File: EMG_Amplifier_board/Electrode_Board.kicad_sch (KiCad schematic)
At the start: 0 parts

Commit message: pcb design v1
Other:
- sheet input_protection_and_decoupling ports: added none; removed GND
- sheet output_protection ports: added none; removed GND

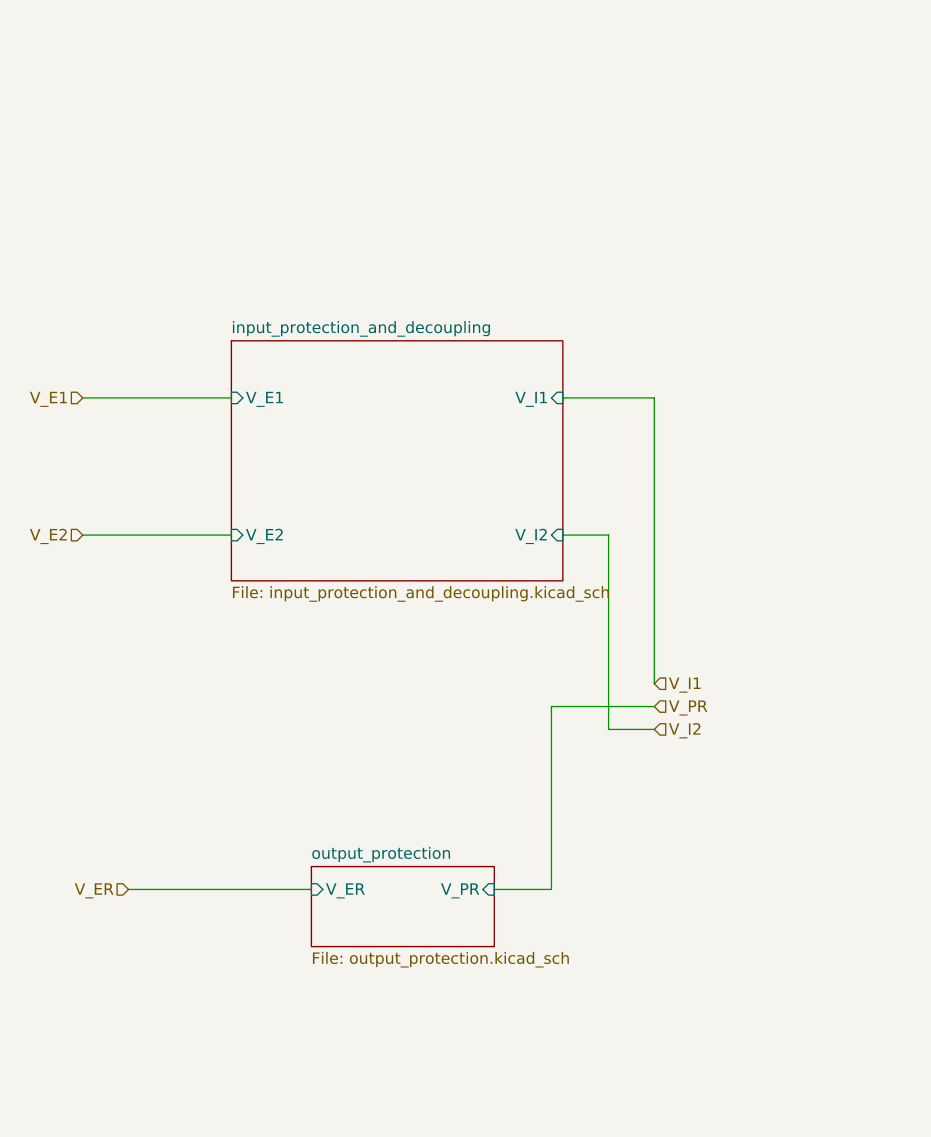
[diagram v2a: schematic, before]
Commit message: update R and C refs to correspond to paper
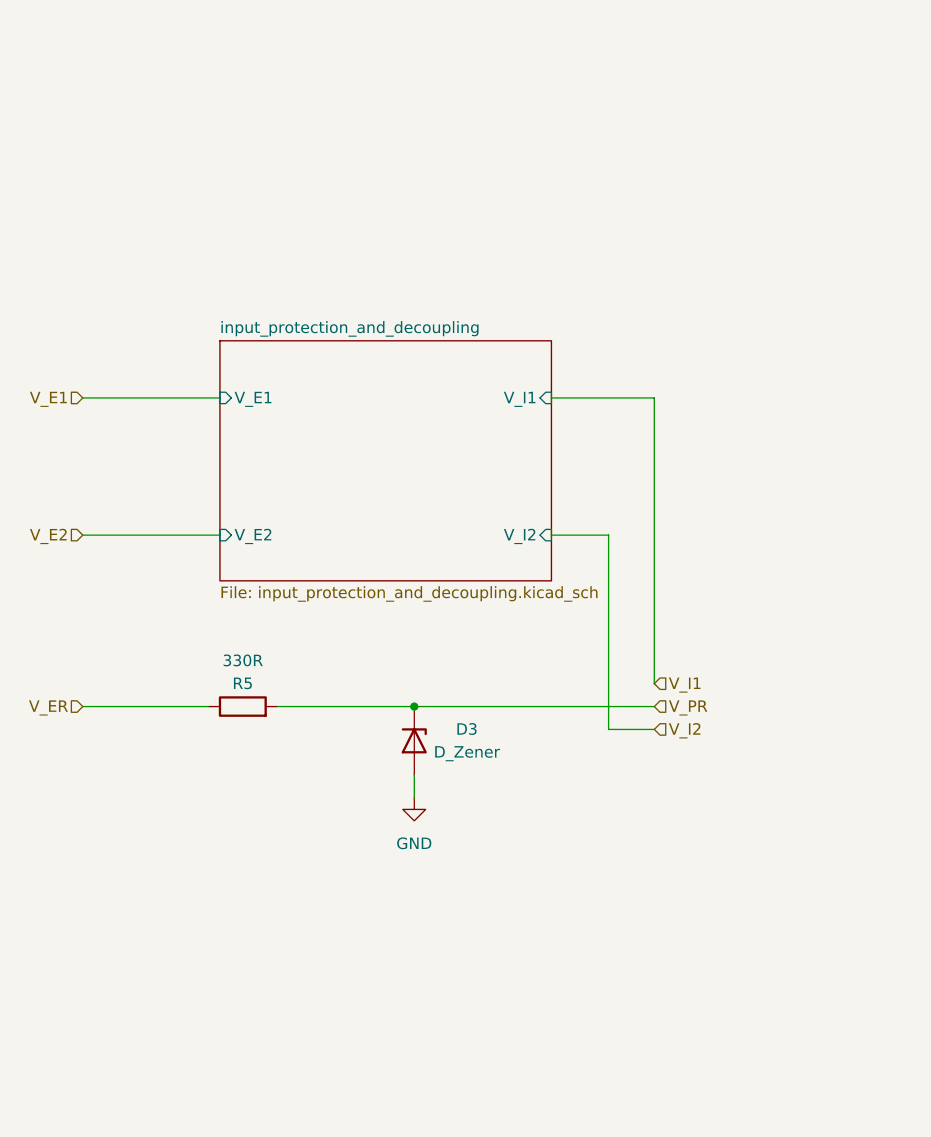
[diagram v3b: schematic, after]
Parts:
- added D3: D_Zener, Diode_SMD:D_SOD-523, symbol Device:D_Zener
- added R5: 330R, Resistor_SMD:R_0402_1005Metric, symbol Device:R
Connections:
- net V_ER: now also R5.1
- net V_PR: now also D3.1 (K), R5.2
- new net GND: D3.2 (A)
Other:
- removed sheet output_protection
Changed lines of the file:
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@@
 	(generator_version "8.0")
 	(paper "A4")
-	(wire
-		(pts
-			(xy 135.89 116.84) (xy 135.89 96.52)
-		)
-		(stroke
-			(width 0)
-			(type default)
-		)
-	)
-	(wire
-		(pts
-			(xy 129.54 116.84) (xy 135.89 116.84)
-		)
-		(stroke
-			(width 0)
-			(type default)
-		)
-	)
-	(wire
-		(pts
-			(xy 137.16 77.47) (xy 142.24 77.47)
-		)
-		(stroke
-			(width 0)
-			(type default)
-		)
-	)
-	(wire
-		(pts
-			(xy 83.82 77.47) (xy 100.33 77.47)
-		)
-		(stroke
-			(width 0)
-			(type default)
-		)
-	)
-	(wire
-		(pts
-			(xy 88.9 116.84) (xy 109.22 116.84)
-		)
-		(stroke
-			(width 0)
-			(type default)
-		)
-	)
-	(wire
-		(pts
-			(xy 135.89 96.52) (xy 147.32 96.52)
+	(junction
+		(at 120.65 96.52)
+		(diameter 0)
+		(color 0 0 0 0)
+	)
+	(wire
+		(pts
+			(xy 120.65 104.14) (xy 120.65 106.68)
+		)
+		(stroke
+			(width 0)
+			(type default)
+		)
+	)
+	(wire
+		(pts
+			(xy 105.41 96.52) (xy 120.65 96.52)
+		)
+		(stroke
+			(width 0)
+			(type default)
+		)
+	)
+	(wire
+		(pts
+			(xy 83.82 96.52) (xy 97.79 96.52)
+		)
+		(stroke
+			(width 0)
+			(type default)
+		)
+	)
+	(wire
+		(pts
+			(xy 135.89 77.47) (xy 142.24 77.47)
+		)
+		(stroke
+			(width 0)
+			(type default)
+		)
+	)
+	(wire
+		(pts
+			(xy 83.82 77.47) (xy 99.06 77.47)
 		)
 		(stroke
@@
 	(wire
 		(pts
-			(xy 137.16 62.23) (xy 147.32 62.23)
-		)
-		(stroke
-			(width 0)
-			(type default)
-		)
-	)
-	(wire
-		(pts
-			(xy 100.33 62.23) (xy 83.82 62.23)
+			(xy 120.65 96.52) (xy 147.32 96.52)
+		)
+		(stroke
+			(width 0)
+			(type default)
+		)
+	)
+	(wire
+		(pts
+			(xy 135.89 62.23) (xy 147.32 62.23)
+		)
+		(stroke
+			(width 0)
+			(type default)
+		)
+	)
+	(wire
+		(pts
+			(xy 99.06 62.23) (xy 83.82 62.23)
 		)
 		(stroke
@@
 		)
 	)
+	(hierarchical_label "V_I2"
+		(shape input)
+		(at 147.32 99.06 0)
+		(fields_autoplaced yes)
+		(effects
+			(font
+				(size 1.27 1.27)
+			)
+			(justify left)
+		)
+	)
 	(hierarchical_label "V_ER"
 		(shape input)
-		(at 88.9 116.84 180)
+		(at 83.82 96.52 180)
 		(fields_autoplaced yes)
 		(effects
@@
 		)
 	)
-	(hierarchical_label "V_I2"
-		(shape input)
-		(at 147.32 99.06 0)
-		(fields_autoplaced yes)
-		(effects
-			(font
-				(size 1.27 1.27)
-			)
-			(justify left)
-		)
-	)
 	(hierarchical_label "V_E1"
 		(shape input)
@@
 		)
 	)
+	(symbol
+		(lib_id "Device:D_Zener")
+		(at 120.65 100.33 270)
+		(unit 1)
+		(exclude_from_sim no)
+		(in_bom yes)
+		(on_board yes)
+		(dnp no)
+		(property "Reference" "D3"
+			(at 126.492 99.06 90)
+			(effects
+				(font
+					(size 1.27 1.27)
+				)
+			)
+		)
+		(property "Value" "D_Zener"
+			(at 126.492 101.6 90)
+			(effects
+				(font
+					(size 1.27 1.27)
+				)
+			)
+		)
+		(property "Footprint" "Diode_SMD:D_SOD-523"
+			(at 120.65 100.33 0)
+			(effects
+				(font
+					(size 1.27 1.27)
+				)
+				(hide yes)
+			)
+		)
+		(property "Datasheet" "~"
+			(at 120.65 100.33 0)
+			(effects
+				(font
+					(size 1.27 1.27)
+				)
+				(hide yes)
+			)
+		)
+		(property "Description" "Zener diode"
+			(at 120.65 100.33 0)
+			(effects
+				(font
+					(size 1.27 1.27)
+				)
+				(hide yes)
+			)
+		)
+		(pin "2"
+		)
+		(pin "1"
+		)
+		(instances
+			(project "EMG_amplifier"
+				(path "/26861adc-1ddf-4c37-9f8b-8db1c0839771/5ea975e8-3227-4877-bc8b-ac5d6b7605f1"
+					(reference "D3")
+					(unit 1)
+				)
+			)
+		)
+	)
+	(symbol
+		(lib_id "Device:R")
+		(at 101.6 96.52 90)
+		(unit 1)
+		(exclude_from_sim no)
+		(in_bom yes)
+		(on_board yes)
+		(dnp no)
+		(property "Reference" "R5"
+			(at 101.6 93.98 90)
+			(effects
+				(font
+					(size 1.27 1.27)
+				)
+			)
+		)
+		(property "Value" "330R"
+			(at 101.6 91.44 90)
+			(effects
+				(font
+					(size 1.27 1.27)
+				)
+			)
+		)
+		(property "Footprint" "Resistor_SMD:R_0402_1005Metric"
+			(at 101.6 98.298 90)
+			(effects
+				(font
+					(size 1.27 1.27)
+				)
+				(hide yes)
+			)
+		)
+		(property "Datasheet" "~"
+			(at 101.6 96.52 0)
+			(effects
+				(font
+					(size 1.27 1.27)
+				)
+				(hide yes)
+			)
+		)
+		(property "Description" "Resistor"
+			(at 101.6 96.52 0)
+			(effects
+				(font
+					(size 1.27 1.27)
+				)
+				(hide yes)
+			)
+		)
+		(pin "1"
+		)
+		(pin "2"
+		)
+		(instances
+			(project "EMG_amplifier"
+				(path "/26861adc-1ddf-4c37-9f8b-8db1c0839771/5ea975e8-3227-4877-bc8b-ac5d6b7605f1"
+					(reference "R5")
+					(unit 1)
+				)
+			)
+		)
+	)
+	(symbol
+		(lib_id "power:GND")
+		(at 120.65 106.68 0)
+		(unit 1)
+		(exclude_from_sim no)
+		(in_bom yes)
+		(on_board yes)
+		(dnp no)
+		(fields_autoplaced yes)
+		(property "Reference" "#PWR01"
+			(at 120.65 113.03 0)
+			(effects
+				(font
+					(size 1.27 1.27)
+				)
+				(hide yes)
+			)
+		)
+		(property "Value" "GND"
+			(at 120.65 111.76 0)
+			(effects
+				(font
+					(size 1.27 1.27)
+				)
+			)
+		)
+		(property "Footprint" ""
+			(at 120.65 106.68 0)
+			(effects
+				(font
+					(size 1.27 1.27)
+				)
+				(hide yes)
+			)
+		)
+		(property "Datasheet" ""
+			(at 120.65 106.68 0)
+			(effects
+				(font
+					(size 1.27 1.27)
+				)
+				(hide yes)
+			)
+		)
+		(property "Description" "Power symbol creates a global label with name \"GND\" , ground"
+			(at 120.65 106.68 0)
+			(effects
+				(font
+					(size 1.27 1.27)
+				)
+				(hide yes)
+			)
+		)
+		(pin "1"
+		)
+		(instances
+			(project "EMG_amplifier"
+				(path "/26861adc-1ddf-4c37-9f8b-8db1c0839771/5ea975e8-3227-4877-bc8b-ac5d6b7605f1"
+					(reference "#PWR01")
+					(unit 1)
+				)
+			)
+		)
+	)
 	(sheet
-		(at 100.33 55.88)
+		(at 99.06 55.88)
 		(size 36.83 26.67)
 		(fields_autoplaced yes)
@@
 		)
 		(property "Sheetname" "input_protection_and_decoupling"
-			(at 100.33 55.1684 0)
+			(at 99.06 55.1684 0)
 			(effects
 				(font
@@
 		)
 		(property "Sheetfile" "input_protection_and_decoupling.kicad_sch"
-			(at 100.33 83.1346 0)
+			(at 99.06 83.1346 0)
 			(effects
 				(font
@@
 		)
 		(pin "V_E1" input
-			(at 100.33 62.23 180)
+			(at 99.06 62.23 180)
 			(effects
 				(font
@@
 		)
 		(pin "V_E2" input
-			(at 100.33 77.47 180)
+			(at 99.06 77.47 180)
 			(effects
 				(font
@@
 		)
 		(pin "V_I1" input
-			(at 137.16 62.23 0)
+			(at 135.89 62.23 0)
 			(effects
 				(font
@@
 		)
 		(pin "V_I2" input
-			(at 137.16 77.47 0)
+			(at 135.89 77.47 0)
 			(effects
 				(font
@@
 				)
 			)
-		)
-	)
-	(sheet
-		(at 109.22 114.3)
-		(size 20.32 8.89)
-		(fields_autoplaced yes)
-		(stroke
-			(width 0.1524)
-			(type solid)
-		)
-		(fill
-			(color 0 0 0 0.0000)
-		)
-		(property "Sheetname" "output_protection"
-			(at 109.22 113.5884 0)
-			(effects
-				(font
-					(size 1.27 1.27)
-				)
-				(justify left bottom)
-			)
-		)
-		(property "Sheetfile" "output_protection.kicad_sch"
-			(at 109.22 123.7746 0)
-			(effects
-				(font
-					(size 1.27 1.27)
-				)
-				(justify left top)
-			)
-		)
-		(pin "V_PR" input
-			(at 129.54 116.84 0)
-			(effects
-				(font
-					(size 1.27 1.27)
-				)
-				(justify right)
-			)
-		)
-		(pin "V_ER" input
-			(at 109.22 116.84 180)
-			(effects
-				(font
-					(size 1.27 1.27)
-				)
-				(justify left)
-			)
-		)
-		(instances
-			(project "EMG_amplifier"
-				(path "/26861adc-1ddf-4c37-9f8b-8db1c0839771/5ea975e8-3227-4877-bc8b-ac5d6b7605f1"
-					(page "6")
-				)
-			)

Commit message: replace 2012 capacitors with 1005
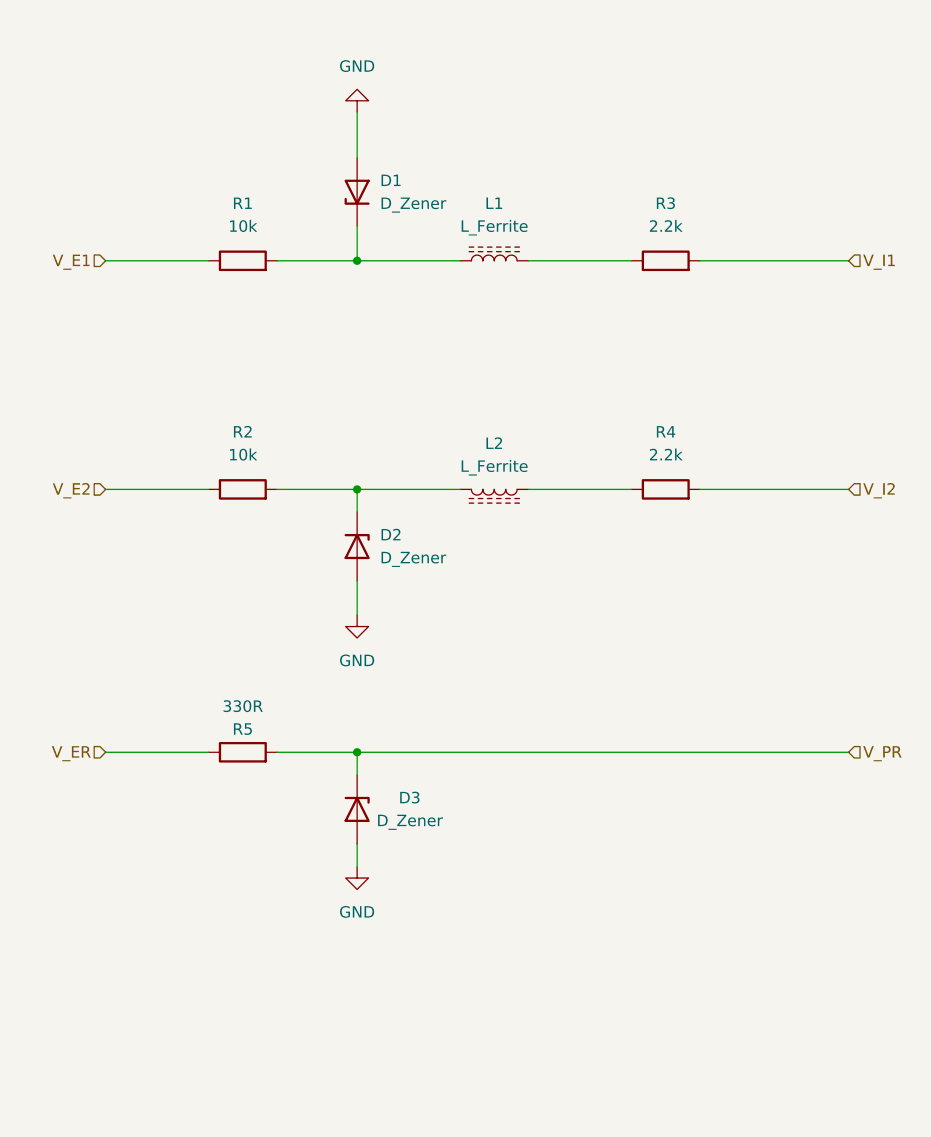
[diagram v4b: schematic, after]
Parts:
- added D1, D2: D_Zener, Diode_SMD:D_SOD-523, symbol Device:D_Zener
- added L1, L2: L_Ferrite, BLM15AX102SN1D_footprints:IND_BLM15_1P05X0P55X0P55_MUR, symbol Device:L_Ferrite
- added R1, R2: 10k, Resistor_SMD:R_0402_1005Metric, symbol Device:R
- added R3, R4: 2.2k, Resistor_SMD:R_0402_1005Metric, symbol Device:R
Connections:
- net GND: now also D1.2 (A), D2.2 (A)
- net V_E1: now also R1.1
- net V_E2: now also R2.1
- net V_I1: now also R3.2
- net V_I2: now also R4.2
- new net: D1.1 (K), L1.1, R1.2
- new net: L1.2, R3.1
- new net: D2.1 (K), L2.2, R2.2
- new net: L2.1, R4.1
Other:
- removed sheet input_protection_and_decoupling
- moved on the sheet: D3, R5

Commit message: update ferrite beads' and zener diodes' footprints
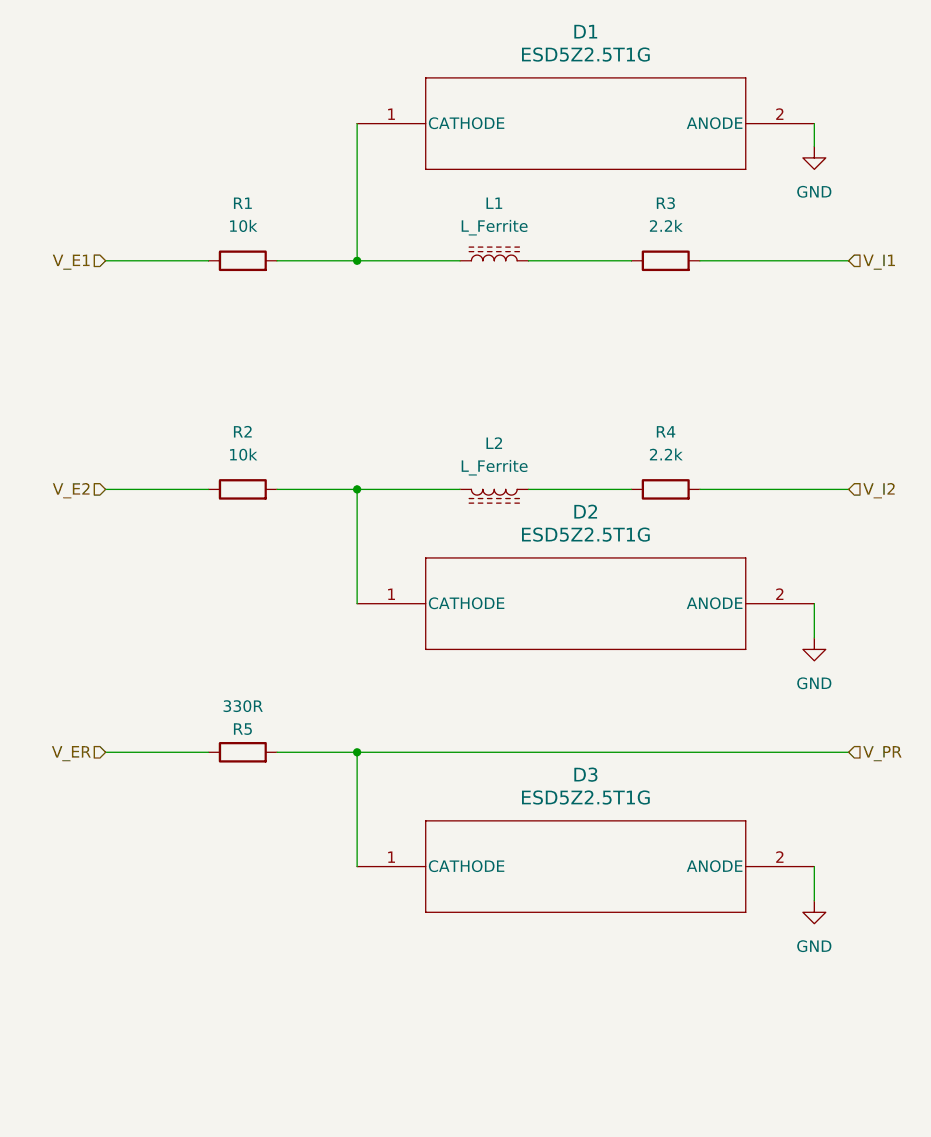
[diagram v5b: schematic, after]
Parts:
- removed D1, D2, D3: D_Zener, Diode_SMD:D_SOD-523, symbol Device:D_Zener
- added D1, D2, D3: ESD5Z2.5T1G, SOD-523_0P9X1P3_ONS, symbol ESD5Z2.5T1G:ESD5Z2.5T1G
- L1, L2: footprint BLM15AX102SN1D_footprints:IND_BLM15_1P05X0P55X0P55_MUR -> BLM15AX102SN1D:IND_BLM15_1P05X0P55X0P55_MUR
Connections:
- net GND: now also D1.2 (ANODE), D2.2 (ANODE), D3.2 (ANODE)
- net V_PR: now also D3.1 (CATHODE)
- net at L1.1, R1.2: now also D1.1 (CATHODE)
- net at L2.2, R2.2: now also D2.1 (CATHODE)
